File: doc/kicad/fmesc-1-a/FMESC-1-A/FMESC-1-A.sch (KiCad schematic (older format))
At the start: 0 parts

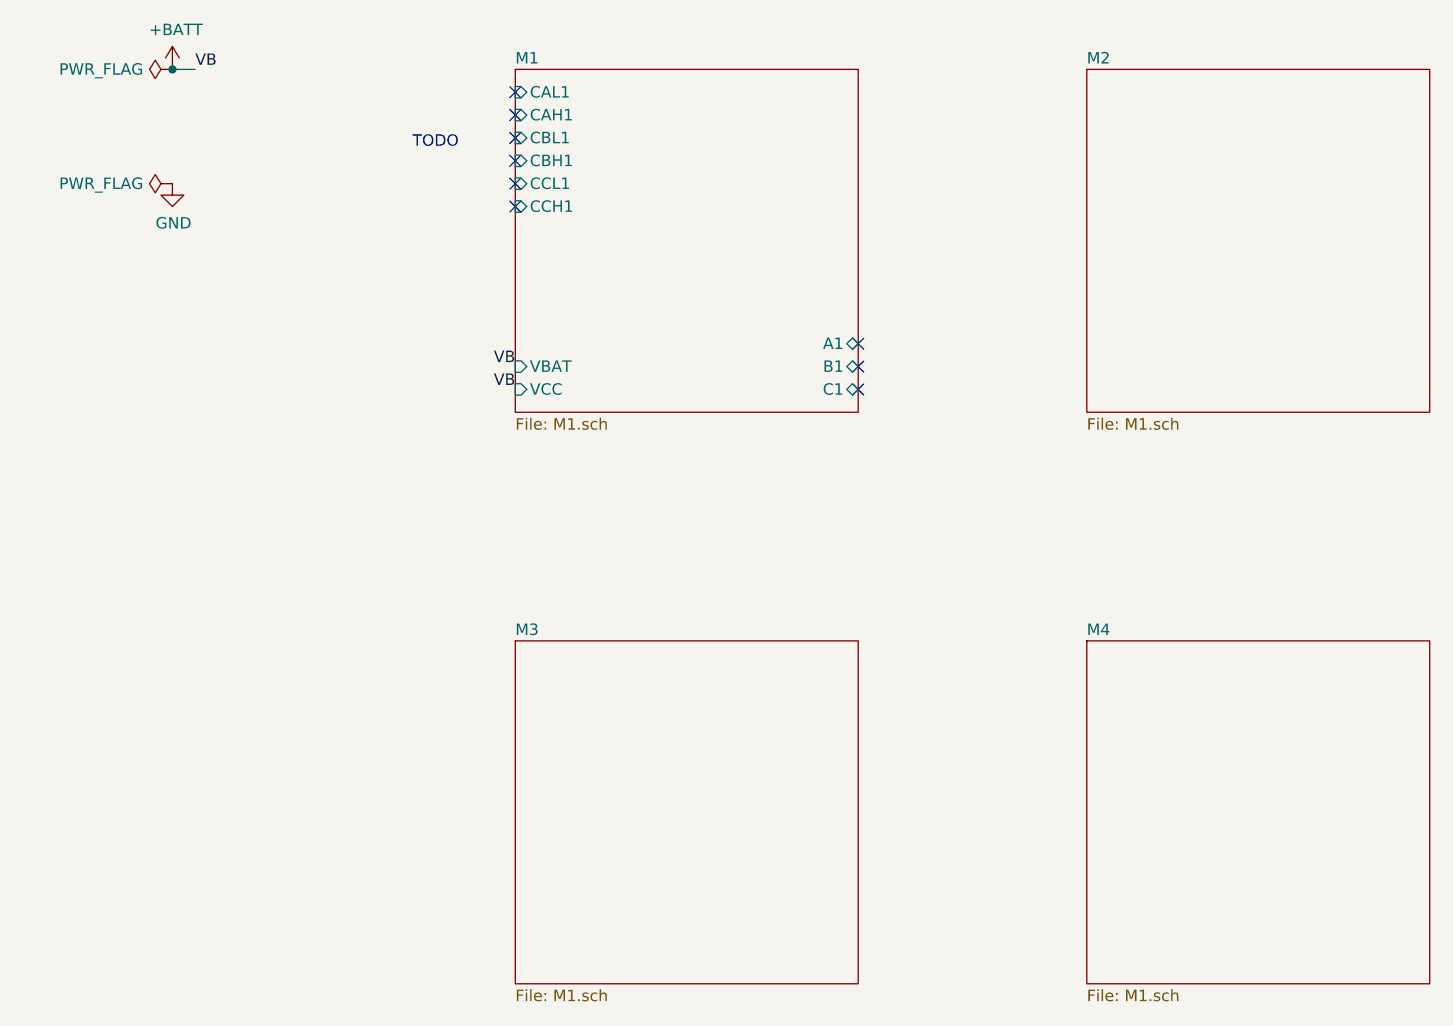
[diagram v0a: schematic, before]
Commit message: doc/kicad: FMESC-1-A  add DFN5x6_8L_EP1_P.kicad_mod
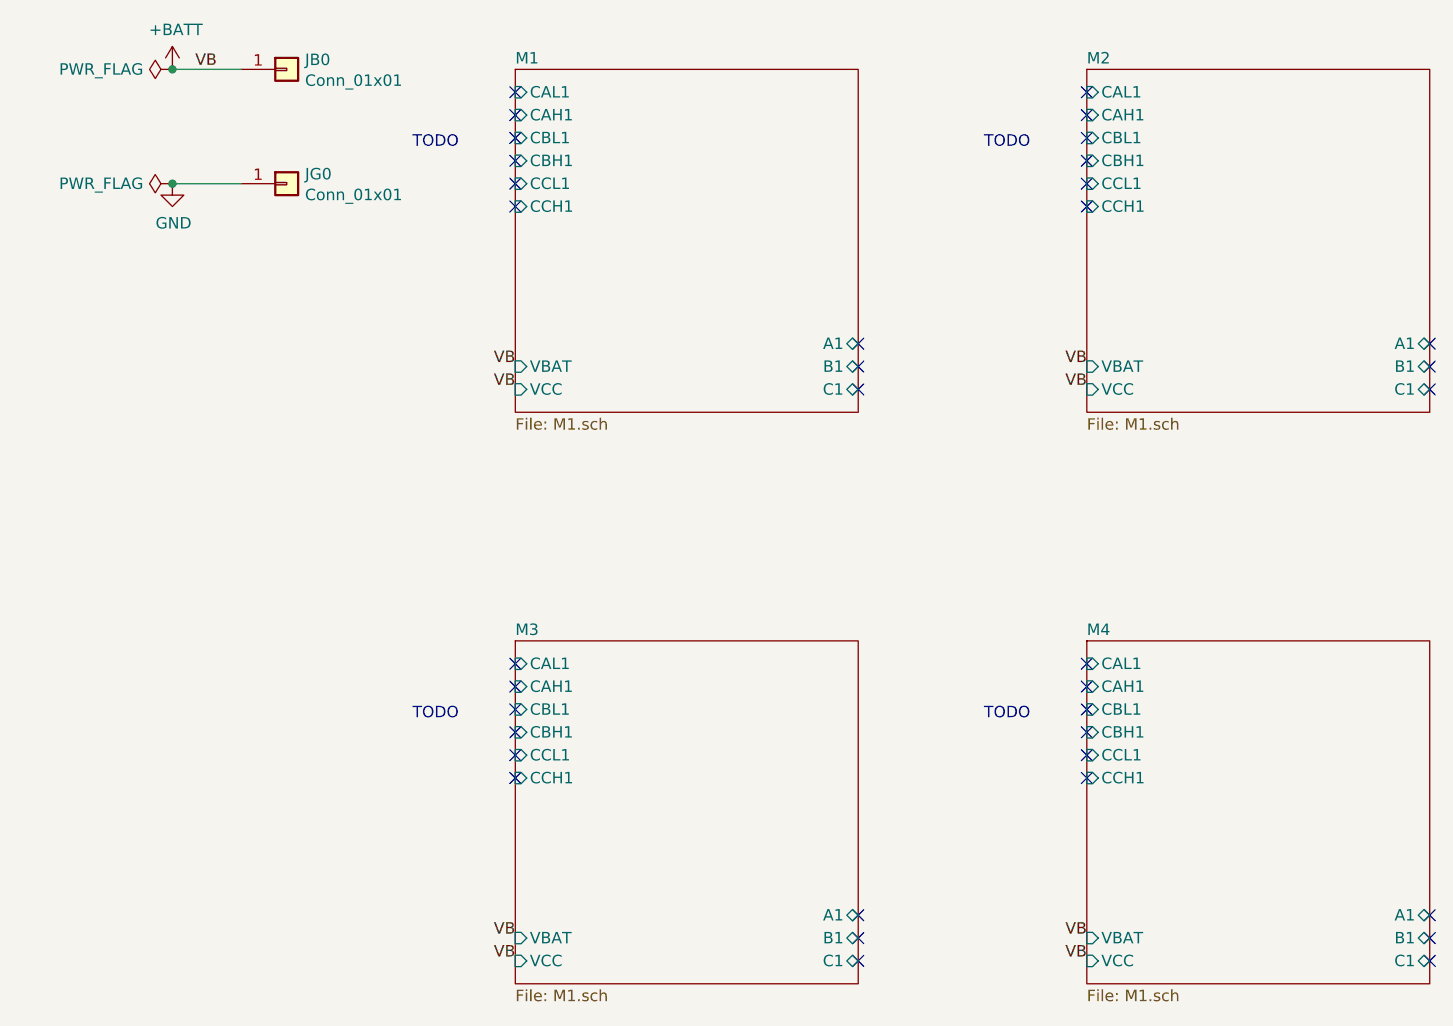
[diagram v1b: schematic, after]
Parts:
- added JB0: Conn_01x01, fmlibf:JS4x8mm, symbol Connector_Generic:Conn_01x01
- added JG0: Conn_01x01, fmlibf:JS8x8mm, symbol Connector_Generic:Conn_01x01
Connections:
- net +BATT: now also JB0.1 (Pin_1)
- net GND: now also JG0.1 (Pin_1)
- no-connect marks 9 -> 36
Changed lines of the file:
@@
 Sheet 1 5
 Title "FMESC-1-A"
-Date "2020-11-03"
+Date "2020-11-05"
 Rev "TODO"
 Comp "sceext"
@@
 $EndDescr
 $Comp
-L power:+BATT #PWR?
+L power:+BATT #PWR0101
 U 1 1 5FA17820
 P 1500 1500
-F 0 "#PWR?" H 1500 1350 50  0001 C CNN
+F 0 "#PWR0101" H 1500 1350 50  0001 C CNN
 F 1 "+BATT" H 1515 1673 50  0000 C CNN
 F 2 "" H 1500 1500 50  0001 C CNN
@@
 $EndComp
 $Comp
-L power:GND #PWR?
+L power:GND #PWR0102
 U 1 1 5FA17AEC
 P 1500 2000
-F 0 "#PWR?" H 1500 1750 50  0001 C CNN
+F 0 "#PWR0102" H 1500 1750 50  0001 C CNN
 F 1 "GND" H 1505 1827 50  0000 C CNN
 F 2 "" H 1500 2000 50  0001 C CNN
@@
 $EndComp
 $Comp
-L power:PWR_FLAG #FLG?
+L power:PWR_FLAG #FLG0101
 U 1 1 5FA17FCC
 P 1500 1500
-F 0 "#FLG?" H 1500 1575 50  0001 C CNN
+F 0 "#FLG0101" H 1500 1575 50  0001 C CNN
 F 1 "PWR_FLAG" V 1500 1627 50  0000 L CNN
 F 2 "" H 1500 1500 50  0001 C CNN
@@
 $EndComp
 $Comp
-L power:PWR_FLAG #FLG?
+L power:PWR_FLAG #FLG0102
 U 1 1 5FA180FB
 P 1500 2000
-F 0 "#FLG?" H 1500 2075 50  0001 C CNN
+F 0 "#FLG0102" H 1500 2075 50  0001 C CNN
 F 1 "PWR_FLAG" V 1500 2127 50  0000 L CNN
 F 2 "" H 1500 2000 50  0001 C CNN
@@
 F12 "C1" B R 4500 2900 50
 $EndSheet
-$Sheet
-S 5500 1500 1500 1500
-U 5FA433EC
-F0 "M2" 50
-F1 "M1.sch" 50
-$EndSheet
-$Sheet
-S 3000 4000 1500 1500
-U 5FA435C0
-F0 "M3" 50
-F1 "M1.sch" 50
-$EndSheet
-$Sheet
-S 5500 4000 1500 1500
-U 5FA4361C
-F0 "M4" 50
-F1 "M1.sch" 50
-$EndSheet
 Text Notes 2550 1850 0    50   ~ 0
 TODO\n
 Text Label 1600 1500 0    50   ~ 0
 VB
-Wire Wire Line
-	1600 1500 1500 1500
 Connection ~ 1500 1500
 Text Label 3000 2800 2    50   ~ 0
@@
 NoConn ~ 4500 2800
 NoConn ~ 4500 2900
+$Sheet
+S 5500 1500 1500 1500
+U 5FA3E74F
+F0 "M2" 50
+F1 "M1.sch" 50
+F2 "CAL1" I L 5500 1600 50
+F3 "CBL1" I L 5500 1800 50
+F4 "CCL1" I L 5500 2000 50
+F5 "CAH1" I L 5500 1700 50
+F6 "CBH1" I L 5500 1900 50
+F7 "CCH1" I L 5500 2100 50
+F8 "VBAT" I L 5500 2800 50
+F9 "VCC" I L 5500 2900 50
+F10 "A1" B R 7000 2700 50
+F11 "B1" B R 7000 2800 50
+F12 "C1" B R 7000 2900 50
+$EndSheet
+Text Notes 5050 1850 0    50   ~ 0
+TODO\n
+Text Label 5500 2800 2    50   ~ 0
+VB
+Text Label 5500 2900 2    50   ~ 0
+VB
+NoConn ~ 5500 1600
+NoConn ~ 5500 1700
+NoConn ~ 5500 1800
+NoConn ~ 5500 1900
+NoConn ~ 5500 2000
+NoConn ~ 5500 2100
+NoConn ~ 7000 2700
+NoConn ~ 7000 2800
+NoConn ~ 7000 2900
+$Sheet
+S 3000 4000 1500 1500
+U 5FA3EBFA
+F0 "M3" 50
+F1 "M1.sch" 50
+F2 "CAL1" I L 3000 4100 50
+F3 "CBL1" I L 3000 4300 50
+F4 "CCL1" I L 3000 4500 50
+F5 "CAH1" I L 3000 4200 50
+F6 "CBH1" I L 3000 4400 50
+F7 "CCH1" I L 3000 4600 50
+F8 "VBAT" I L 3000 5300 50
+F9 "VCC" I L 3000 5400 50
+F10 "A1" B R 4500 5200 50
+F11 "B1" B R 4500 5300 50
+F12 "C1" B R 4500 5400 50
+$EndSheet
+Text Notes 2550 4350 0    50   ~ 0
+TODO\n
+Text Label 3000 5300 2    50   ~ 0
+VB
+Text Label 3000 5400 2    50   ~ 0
+VB
+NoConn ~ 3000 4100
+NoConn ~ 3000 4200
+NoConn ~ 3000 4300
+NoConn ~ 3000 4400
+NoConn ~ 3000 4500
+NoConn ~ 3000 4600
+NoConn ~ 4500 5200
+NoConn ~ 4500 5300
+NoConn ~ 4500 5400
+$Sheet
+S 5500 4000 1500 1500
+U 5FA3F05C
+F0 "M4" 50
+F1 "M1.sch" 50
+F2 "CAL1" I L 5500 4100 50
+F3 "CBL1" I L 5500 4300 50
+F4 "CCL1" I L 5500 4500 50
+F5 "CAH1" I L 5500 4200 50
+F6 "CBH1" I L 5500 4400 50
+F7 "CCH1" I L 5500 4600 50
+F8 "VBAT" I L 5500 5300 50
+F9 "VCC" I L 5500 5400 50
+F10 "A1" B R 7000 5200 50
+F11 "B1" B R 7000 5300 50
+F12 "C1" B R 7000 5400 50
+$EndSheet
+Text Notes 5050 4350 0    50   ~ 0
+TODO\n
+Text Label 5500 5300 2    50   ~ 0
+VB
+Text Label 5500 5400 2    50   ~ 0
+VB
+NoConn ~ 5500 4100
+NoConn ~ 5500 4200
+NoConn ~ 5500 4300
+NoConn ~ 5500 4400
+NoConn ~ 5500 4500
+NoConn ~ 5500 4600
+NoConn ~ 7000 5200
+NoConn ~ 7000 5300
+NoConn ~ 7000 5400
+$Comp
+L Connector_Generic:Conn_01x01 JB0
+U 1 1 5FA4066F
+P 2000 1500
+F 0 "JB0" H 2080 1542 50  0000 L CNN
+F 1 "Conn_01x01" H 2080 1451 50  0000 L CNN
+F 2 "fmlibf:JS4x8mm" H 2000 1500 50  0001 C CNN
+F 3 "~" H 2000 1500 50  0001 C CNN
+	1    2000 1500
+	1    0    0    -1
+$EndComp
+$Comp
+L Connector_Generic:Conn_01x01 JG0
+U 1 1 5FA40896
+P 2000 2000
+F 0 "JG0" H 2080 2042 50  0000 L CNN
+F 1 "Conn_01x01" H 2080 1951 50  0000 L CNN
+F 2 "fmlibf:JS8x8mm" H 2000 2000 50  0001 C CNN
+F 3 "~" H 2000 2000 50  0001 C CNN
+	1    2000 2000
+	1    0    0    -1
+$EndComp
+Wire Wire Line
+	1500 1500 1800 1500
+Wire Wire Line
+	1800 2000 1500 2000
+Connection ~ 1500 2000
 $EndSCHEMATC

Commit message: doc/kicad: FMESC-1-A  update PCB
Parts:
- JB0: footprint fmlibf:JS4x8mm -> fmlibf:JS4x10mm
- JG0: footprint fmlibf:JS8x8mm -> fmlibf:JS4x16mm
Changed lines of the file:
@@
 Sheet 1 5
 Title "FMESC-1-A"
-Date "2020-11-05"
+Date "2020-11-07"
 Rev "TODO"
 Comp "sceext"
@@
 F6 "CBH1" I L 3000 1900 50
 F7 "CCH1" I L 3000 2100 50
-F8 "VBAT" I L 3000 2800 50
-F9 "VCC" I L 3000 2900 50
-F10 "A1" B R 4500 2700 50
-F11 "B1" B R 4500 2800 50
-F12 "C1" B R 4500 2900 50
+F8 "VCC" I L 3000 2900 50
+F9 "A1" B R 4500 2700 50
+F10 "B1" B R 4500 2800 50
+F11 "C1" B R 4500 2900 50
 $EndSheet
 Text Notes 2550 1850 0    50   ~ 0
@@
 VB
 Connection ~ 1500 1500
-Text Label 3000 2800 2    50   ~ 0
-VB
 Text Label 3000 2900 2    50   ~ 0
 VB
@@
 F6 "CBH1" I L 5500 1900 50
 F7 "CCH1" I L 5500 2100 50
-F8 "VBAT" I L 5500 2800 50
-F9 "VCC" I L 5500 2900 50
-F10 "A1" B R 7000 2700 50
-F11 "B1" B R 7000 2800 50
-F12 "C1" B R 7000 2900 50
+F8 "VCC" I L 5500 2900 50
+F9 "A1" B R 7000 2700 50
+F10 "B1" B R 7000 2800 50
+F11 "C1" B R 7000 2900 50
 $EndSheet
 Text Notes 5050 1850 0    50   ~ 0
 TODO\n
-Text Label 5500 2800 2    50   ~ 0
-VB
 Text Label 5500 2900 2    50   ~ 0
 VB
@@
 F6 "CBH1" I L 3000 4400 50
 F7 "CCH1" I L 3000 4600 50
-F8 "VBAT" I L 3000 5300 50
-F9 "VCC" I L 3000 5400 50
-F10 "A1" B R 4500 5200 50
-F11 "B1" B R 4500 5300 50
-F12 "C1" B R 4500 5400 50
+F8 "VCC" I L 3000 5400 50
+F9 "A1" B R 4500 5200 50
+F10 "B1" B R 4500 5300 50
+F11 "C1" B R 4500 5400 50
 $EndSheet
 Text Notes 2550 4350 0    50   ~ 0
 TODO\n
-Text Label 3000 5300 2    50   ~ 0
-VB
 Text Label 3000 5400 2    50   ~ 0
 VB
@@
 F6 "CBH1" I L 5500 4400 50
 F7 "CCH1" I L 5500 4600 50
-F8 "VBAT" I L 5500 5300 50
-F9 "VCC" I L 5500 5400 50
-F10 "A1" B R 7000 5200 50
-F11 "B1" B R 7000 5300 50
-F12 "C1" B R 7000 5400 50
+F8 "VCC" I L 5500 5400 50
+F9 "A1" B R 7000 5200 50
+F10 "B1" B R 7000 5300 50
+F11 "C1" B R 7000 5400 50
 $EndSheet
 Text Notes 5050 4350 0    50   ~ 0
 TODO\n
-Text Label 5500 5300 2    50   ~ 0
-VB
 Text Label 5500 5400 2    50   ~ 0
 VB
@@
 F 0 "JB0" H 2080 1542 50  0000 L CNN
 F 1 "Conn_01x01" H 2080 1451 50  0000 L CNN
-F 2 "fmlibf:JS4x8mm" H 2000 1500 50  0001 C CNN
+F 2 "fmlibf:JS4x10mm" H 2000 1500 50  0001 C CNN
 F 3 "~" H 2000 1500 50  0001 C CNN
 	1    2000 1500
@@
 F 0 "JG0" H 2080 2042 50  0000 L CNN
 F 1 "Conn_01x01" H 2080 1951 50  0000 L CNN
-F 2 "fmlibf:JS8x8mm" H 2000 2000 50  0001 C CNN
+F 2 "fmlibf:JS4x16mm" H 2000 2000 50  0001 C CNN
 F 3 "~" H 2000 2000 50  0001 C CNN
 	1    2000 2000

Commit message: doc/kicad: FMESC-1-A  first PCB layout
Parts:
- JB0: footprint fmlibf:JS4x10mm -> fmlibf:JS3x10mm
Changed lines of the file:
@@
 F 0 "JB0" H 2080 1542 50  0000 L CNN
 F 1 "Conn_01x01" H 2080 1451 50  0000 L CNN
-F 2 "fmlibf:JS4x10mm" H 2000 1500 50  0001 C CNN
+F 2 "fmlibf:JS3x10mm" H 2000 1500 50  0001 C CNN
 F 3 "~" H 2000 1500 50  0001 C CNN
 	1    2000 1500

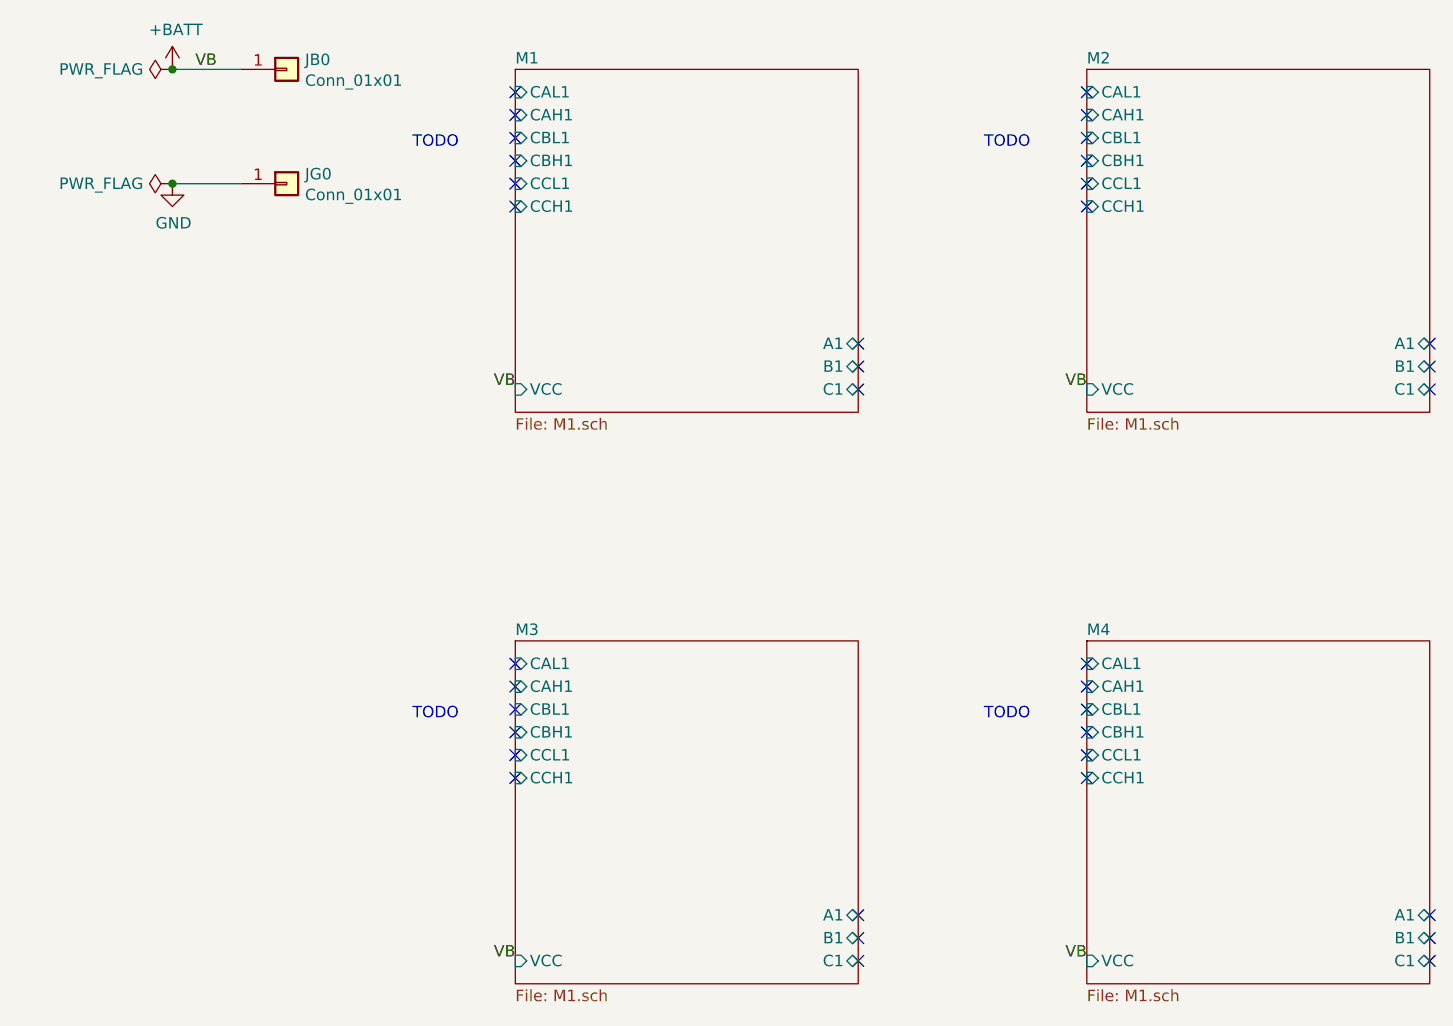
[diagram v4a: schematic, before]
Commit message: doc/kicad: add FMESC-1-C
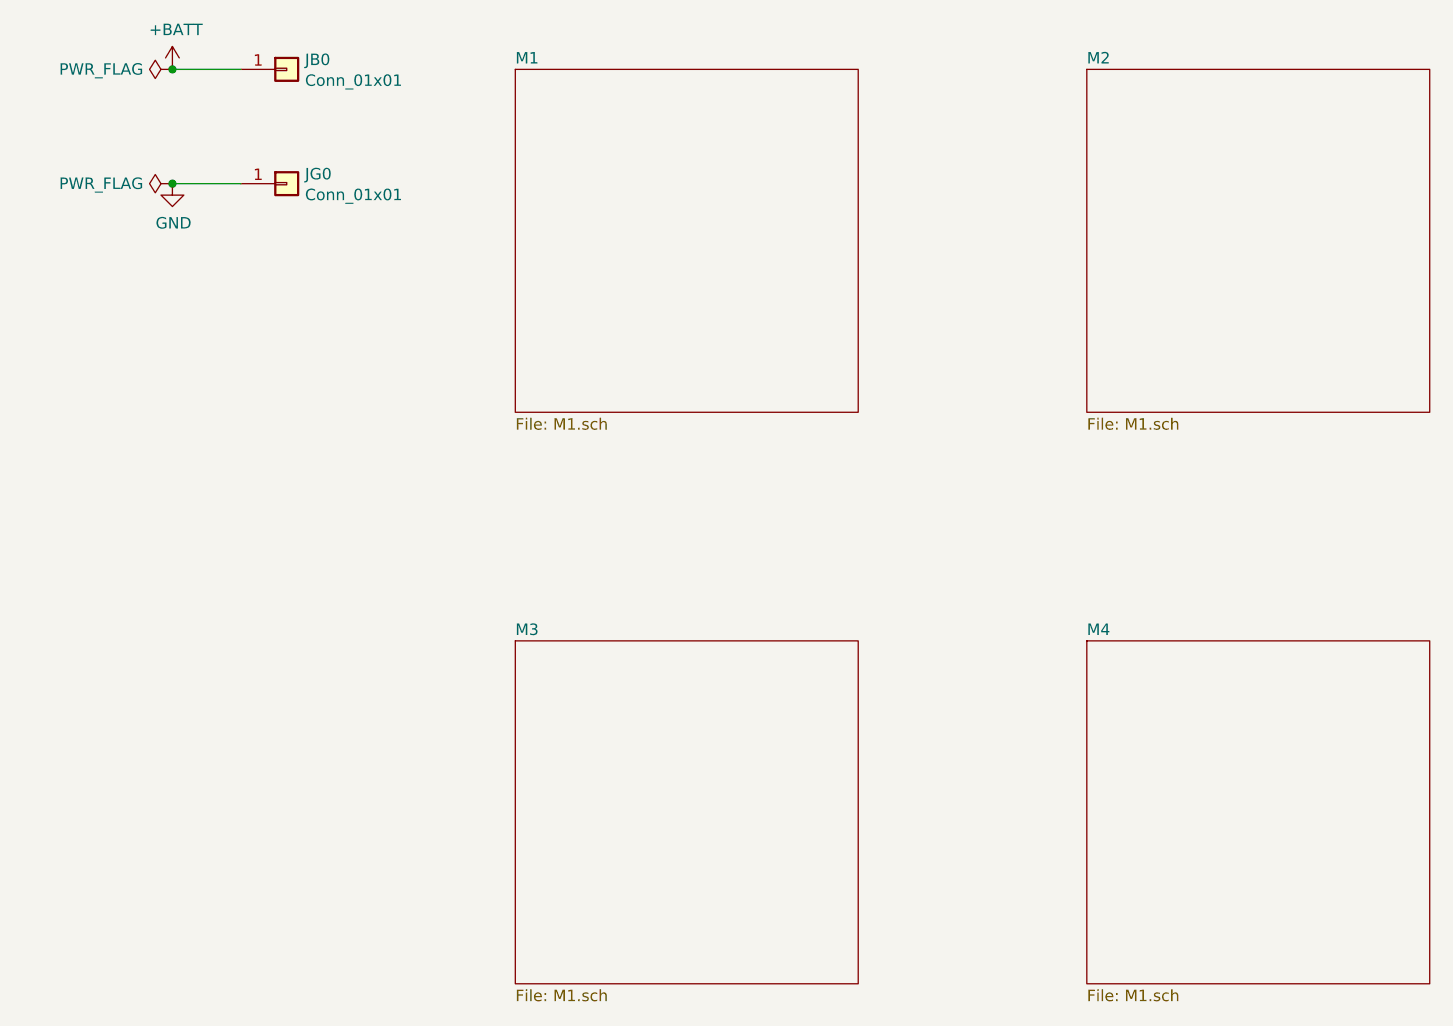
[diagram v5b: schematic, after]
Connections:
- no-connect marks 36 -> 0
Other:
- note removed: "TODO\n"
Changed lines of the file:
@@
 Sheet 1 5
 Title "FMESC-1-A"
-Date "2020-11-07"
+Date "2020-11-08"
 Rev "TODO"
 Comp "sceext"
@@
 	0    -1   -1   0
 $EndComp
-$Sheet
-S 3000 1500 1500 1500
-U 5FA1845D
-F0 "M1" 50
-F1 "M1.sch" 50
-F2 "CAL1" I L 3000 1600 50
-F3 "CBL1" I L 3000 1800 50
-F4 "CCL1" I L 3000 2000 50
-F5 "CAH1" I L 3000 1700 50
-F6 "CBH1" I L 3000 1900 50
-F7 "CCH1" I L 3000 2100 50
-F8 "A1" B R 4500 2700 50
-F9 "B1" B R 4500 2800 50
-F10 "C1" B R 4500 2900 50
-F11 "VCC" I L 3000 2900 50
-$EndSheet
-Text Notes 2550 1850 0    50   ~ 0
-TODO\n
-Text Label 1600 1500 0    50   ~ 0
-VB
 Connection ~ 1500 1500
-Text Label 3000 2900 2    50   ~ 0
-VB
-NoConn ~ 3000 1600
-NoConn ~ 3000 1700
-NoConn ~ 3000 1800
-NoConn ~ 3000 1900
-NoConn ~ 3000 2000
-NoConn ~ 3000 2100
-NoConn ~ 4500 2700
-NoConn ~ 4500 2800
-NoConn ~ 4500 2900
-$Sheet
-S 5500 1500 1500 1500
-U 5FA3E74F
-F0 "M2" 50
-F1 "M1.sch" 50
-F2 "CAL1" I L 5500 1600 50
-F3 "CBL1" I L 5500 1800 50
-F4 "CCL1" I L 5500 2000 50
-F5 "CAH1" I L 5500 1700 50
-F6 "CBH1" I L 5500 1900 50
-F7 "CCH1" I L 5500 2100 50
-F8 "VCC" I L 5500 2900 50
-F9 "A1" B R 7000 2700 50
-F10 "B1" B R 7000 2800 50
-F11 "C1" B R 7000 2900 50
-$EndSheet
-Text Notes 5050 1850 0    50   ~ 0
-TODO\n
-Text Label 5500 2900 2    50   ~ 0
-VB
-NoConn ~ 5500 1600
-NoConn ~ 5500 1700
-NoConn ~ 5500 1800
-NoConn ~ 5500 1900
-NoConn ~ 5500 2000
-NoConn ~ 5500 2100
-NoConn ~ 7000 2700
-NoConn ~ 7000 2800
-NoConn ~ 7000 2900
-$Sheet
-S 3000 4000 1500 1500
-U 5FA3EBFA
-F0 "M3" 50
-F1 "M1.sch" 50
-F2 "CAL1" I L 3000 4100 50
-F3 "CBL1" I L 3000 4300 50
-F4 "CCL1" I L 3000 4500 50
-F5 "CAH1" I L 3000 4200 50
-F6 "CBH1" I L 3000 4400 50
-F7 "CCH1" I L 3000 4600 50
-F8 "VCC" I L 3000 5400 50
-F9 "A1" B R 4500 5200 50
-F10 "B1" B R 4500 5300 50
-F11 "C1" B R 4500 5400 50
-$EndSheet
-Text Notes 2550 4350 0    50   ~ 0
-TODO\n
-Text Label 3000 5400 2    50   ~ 0
-VB
-NoConn ~ 3000 4100
-NoConn ~ 3000 4200
-NoConn ~ 3000 4300
-NoConn ~ 3000 4400
-NoConn ~ 3000 4500
-NoConn ~ 3000 4600
-NoConn ~ 4500 5200
-NoConn ~ 4500 5300
-NoConn ~ 4500 5400
-$Sheet
-S 5500 4000 1500 1500
-U 5FA3F05C
-F0 "M4" 50
-F1 "M1.sch" 50
-F2 "CAL1" I L 5500 4100 50
-F3 "CBL1" I L 5500 4300 50
-F4 "CCL1" I L 5500 4500 50
-F5 "CAH1" I L 5500 4200 50
-F6 "CBH1" I L 5500 4400 50
-F7 "CCH1" I L 5500 4600 50
-F8 "VCC" I L 5500 5400 50
-F9 "A1" B R 7000 5200 50
-F10 "B1" B R 7000 5300 50
-F11 "C1" B R 7000 5400 50
-$EndSheet
-Text Notes 5050 4350 0    50   ~ 0
-TODO\n
-Text Label 5500 5400 2    50   ~ 0
-VB
-NoConn ~ 5500 4100
-NoConn ~ 5500 4200
-NoConn ~ 5500 4300
-NoConn ~ 5500 4400
-NoConn ~ 5500 4500
-NoConn ~ 5500 4600
-NoConn ~ 7000 5200
-NoConn ~ 7000 5300
-NoConn ~ 7000 5400
 $Comp
 L Connector_Generic:Conn_01x01 JB0
@@
 	1800 2000 1500 2000
 Connection ~ 1500 2000
+$Sheet
+S 5500 4000 1500 1500
+U 5FA3F05C
+F0 "M4" 50
+F1 "M1.sch" 50
+$EndSheet
+$Sheet
+S 3000 4000 1500 1500
+U 5FA3EBFA
+F0 "M3" 50
+F1 "M1.sch" 50
+$EndSheet
+$Sheet
+S 5500 1500 1500 1500
+U 5FA3E74F
+F0 "M2" 50
+F1 "M1.sch" 50
+$EndSheet
+$Sheet
+S 3000 1500 1500 1500
+U 5FA1845D
+F0 "M1" 50
+F1 "M1.sch" 50
+$EndSheet
 $EndSCHEMATC
